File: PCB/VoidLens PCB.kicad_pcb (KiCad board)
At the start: 2 copper layers, 75 parts, among them IC1 BMI270, J1 solder pad, J2 JST-XH-2 Pin, J4 JST_XH for led Strip, J5 Programming_Pins, SW1 K3-1391A, SW2 SW_Push_DPDT, SW5 K2-1157SP-I4SW-04, U1 BQ24074RGT, U2 ATmega32U4-M, U3 NRF24L01, U5 TPS61022, U6 TPS27081ADDCR, Y1 16Mhz, Y2 16mhz

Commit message: Arrangeed components to their positions in pcb
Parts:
- R11, R12, U1: moved to B.Cu
- moved U6 127.1 mm to (225.5, 83.5)
- moved U1 117.8 mm to (201.1, 50.9), turned to 180 degrees
- moved R12 76.4 mm to (204.5, 50.9), turned to 90 degrees
- moved L7 26.2 mm to (197.5, 94.5)
- moved C1 23.4 mm to (189.0, 84.5)
- moved C2 23.4 mm to (189.0, 77.5)
- moved J2 23.4 mm to (204.5, 94.0)
- moved J4 23.4 mm to (197.0, 80.0)
- moved J5 23.4 mm to (209.5, 84.1)
- moved SW5 23.4 mm to (190.0, 94.5)
- moved R11 21.3 mm to (197.0, 50.4), turned to 90 degrees
- moved L2 19.9 mm to (107.5, 96.5)
- moved U5 15.3 mm to (208.2, 45.5)
- moved C14 5.73 mm to (167.7, 38.5)
- moved J1 1.74 mm to (196.0, 47.5)
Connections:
- C1 pad 1: batt_main -> Net-(J1-Pin_1)
- C21 pad 1: Net-(U1-IN) -> uvcc
- J1 pad 1: batt_main -> Net-(J1-Pin_1)
- SW1 pad 1: unconnected-(SW1-Pad1) -> Net-(J1-Pin_1)
- SW1 pad 2: Net-(U1-IN) -> batt_main
- SW1 pad 3: uvcc -> unconnected-(SW1-Pad3)
- U1 pad 13: Net-(U1-IN) -> uvcc
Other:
- board text added: "+"
- board text added: "-"

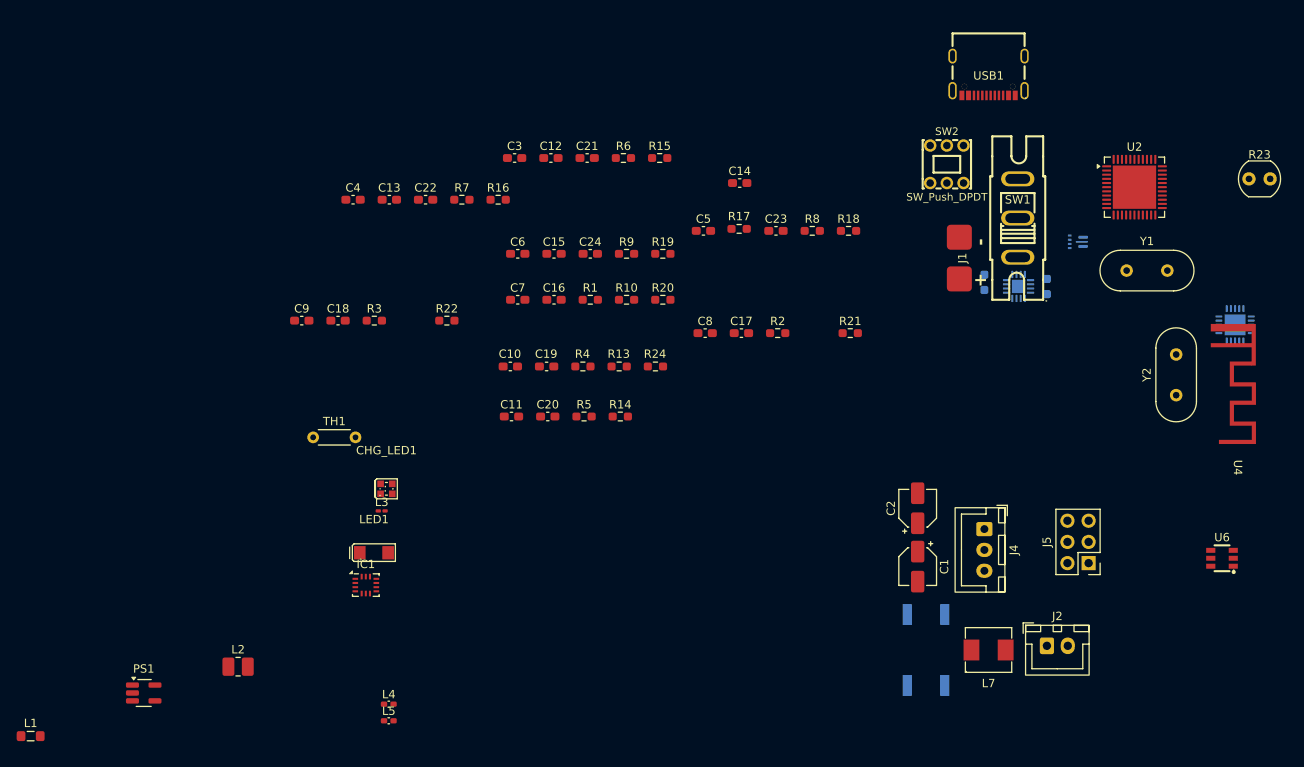
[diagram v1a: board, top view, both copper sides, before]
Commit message: routed more components in the pcb
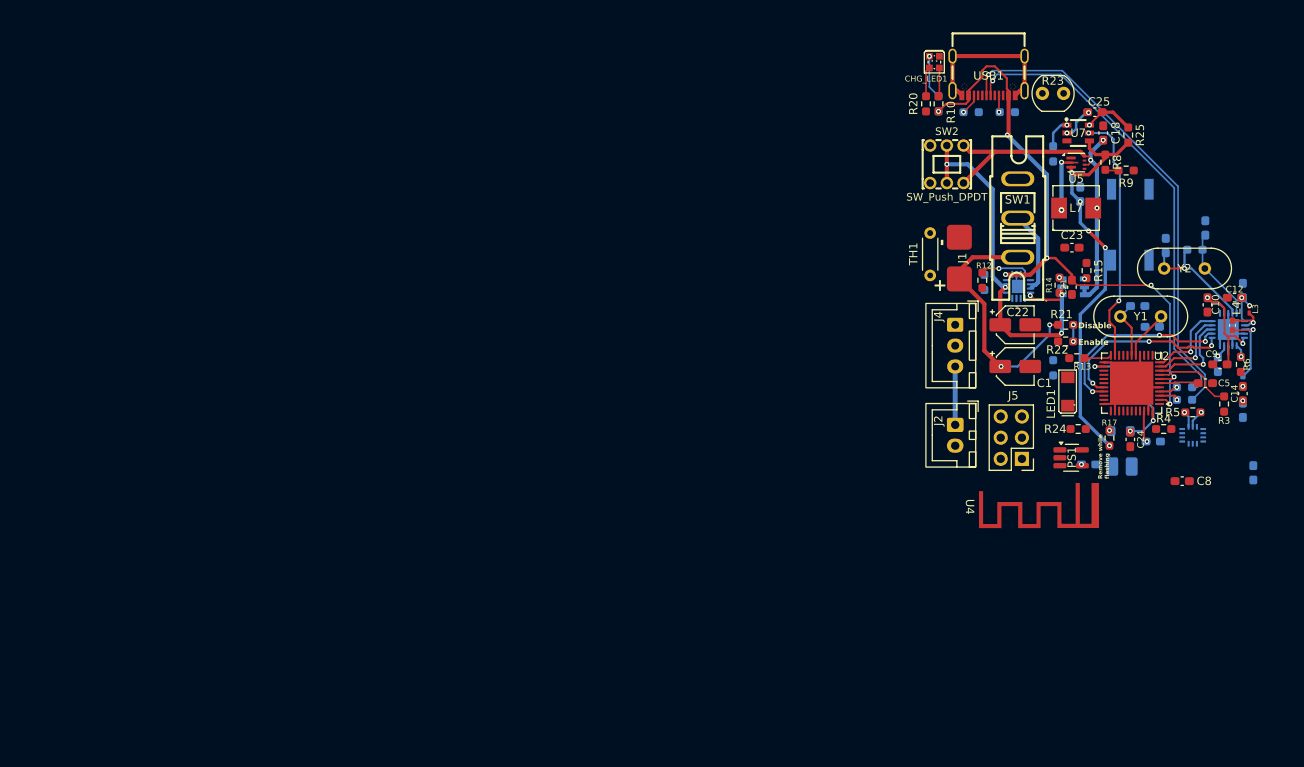
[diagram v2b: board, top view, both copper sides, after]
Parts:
- removed C2: 22uF, Capacitor_SMD:CP_Elec_4x5.4
- added C25: 0.1uF, Capacitor_SMD:C_0603_1608Metric_Pad1.08x0.95mm_HandSolder, F.Cu at (210.2, 30.0)
- added R25: 1k, Resistor_SMD:R_0603_1608Metric_Pad0.98x0.95mm_HandSolder, F.Cu at (214.2, 32.8)
- added R26: 22, Resistor_SMD:R_0603_1608Metric_Pad0.98x0.95mm_HandSolder, B.Cu at (221.0, 63.0)
- added R27: 22, Resistor_SMD:R_0603_1608Metric_Pad0.98x0.95mm_HandSolder, B.Cu at (221.0, 64.5)
- added U7: TPS27081ADDCR, lcsc_footprints:C128404_SOT-23-6_L2_9-W1_6-P0_95-LS2_8-BR, F.Cu at (208.2, 32.5)
- C11, C13, C15, C16, C17, C19, C20, C3, C4, C6, C7, IC1, L1, L2, L5, R1, R16, R19, R2, R7, U6: moved to B.Cu
- C22: footprint Capacitor_SMD:C_0603_1608Metric_Pad1.08x0.95mm_HandSolder -> Capacitor_SMD:CP_Elec_4x5.4
- R12, U5: moved to F.Cu
- R18: value 10k -> 12k; moved to B.Cu
- R3: value 110 -> 1.18k
- moved L1 135.7 mm to (213.3, 68.2)
- moved PS1 114.7 mm to (207.4, 71.5)
- moved L4 110.9 mm to (226.8, 55.6), turned to -90 degrees
- moved C9 110.2 mm to (225.2, 60.2), turned to 180 degrees
- moved L5 110.2 mm to (228.0, 62.2), turned to -90 degrees
- moved L2 108.7 mm to (213.5, 72.5)
- moved L3 106.8 mm to (228.8, 53.7), turned to 90 degrees
- moved C13 102.9 mm to (228.0, 51.4), turned to -90 degrees
- moved R3 102.4 mm to (225.8, 65.0), turned to -90 degrees
- moved IC1 100.8 mm to (222.0, 68.8), turned to 180 degrees
- moved C4 97.1 mm to (217.1, 55.8), turned to 180 degrees
- moved C18 94.5 mm to (211.2, 32.5), turned to 90 degrees
- moved C6 92.0 mm to (229.2, 73.2), turned to 90 degrees
- moved R7 88.1 mm to (222.2, 46.5), turned to 180 degrees
- moved LED1 85.4 mm to (207.0, 63.5), turned to 90 degrees
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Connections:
- C1 pad 1: Net-(J1-Pin_1) -> BQ_E
- J1 pad 1: Net-(J1-Pin_1) -> BQ_E
- R14 pad 1: GND -> Regulated_batt
- R14 pad 2: Net-(U6-R2) -> Net-(U6-R1/C1)
- R15 pad 1: Net-(U6-R1/C1) -> GND
- R15 pad 2: Regulated_batt -> Net-(U6-R2)
- R18 pad 1: 5v_en -> GND
- R18 pad 2: GND -> Net-(U7-R2)
- R21 pad 1: uvcc -> BQ_E
- SW1 pad 1: Net-(J1-Pin_1) -> BQ_E
- U2 pad 3: d- -> Net-(U2-D-)
- U2 pad 4: d+ -> Net-(U2-D+)
- U3 pad 6: IRQ -> unconnected-(U3-IRQ-Pad6)
- U5 pad 5: 5v_en -> +BATT
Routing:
- net uvcc: track 0.00 -> 75.7 mm, vias 0 -> 7
- net d-: track 0.00 -> 58.7 mm, vias 0 -> 1
- net d+: track 0.00 -> 56.1 mm, vias 0 -> 1
- net GND: track 0.00 -> 53.4 mm
- net mcu_5v: track 0.00 -> 49.6 mm, vias 0 -> 5
- net +BATT: track 0.00 -> 43.9 mm, vias 0 -> 3
- net Regulated_batt: track 0.00 -> 41.8 mm, vias 0 -> 4
- net BQ_E: track 0.00 -> 30.9 mm, vias 0 -> 2
- net 5v_en: track 0.00 -> 30.3 mm, vias 0 -> 2
- net CSN: track 0.00 -> 23.2 mm, vias 0 -> 3
- net CE: track 0.00 -> 21.7 mm, vias 0 -> 3
- net +3.3V: track 0.00 -> 16.9 mm, vias 0 -> 3
- net Net-(C24-Pad1): track 0.00 -> 16.1 mm, vias 0 -> 3
- net Net-(U3-XC2): track 0.00 -> 15.0 mm, vias 0 -> 1
- net Net-(U3-XC1): track 0.00 -> 11.2 mm
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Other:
- board text added: "Disable"
- board text added: "Enable"
- board text added: "Remove while flashing"

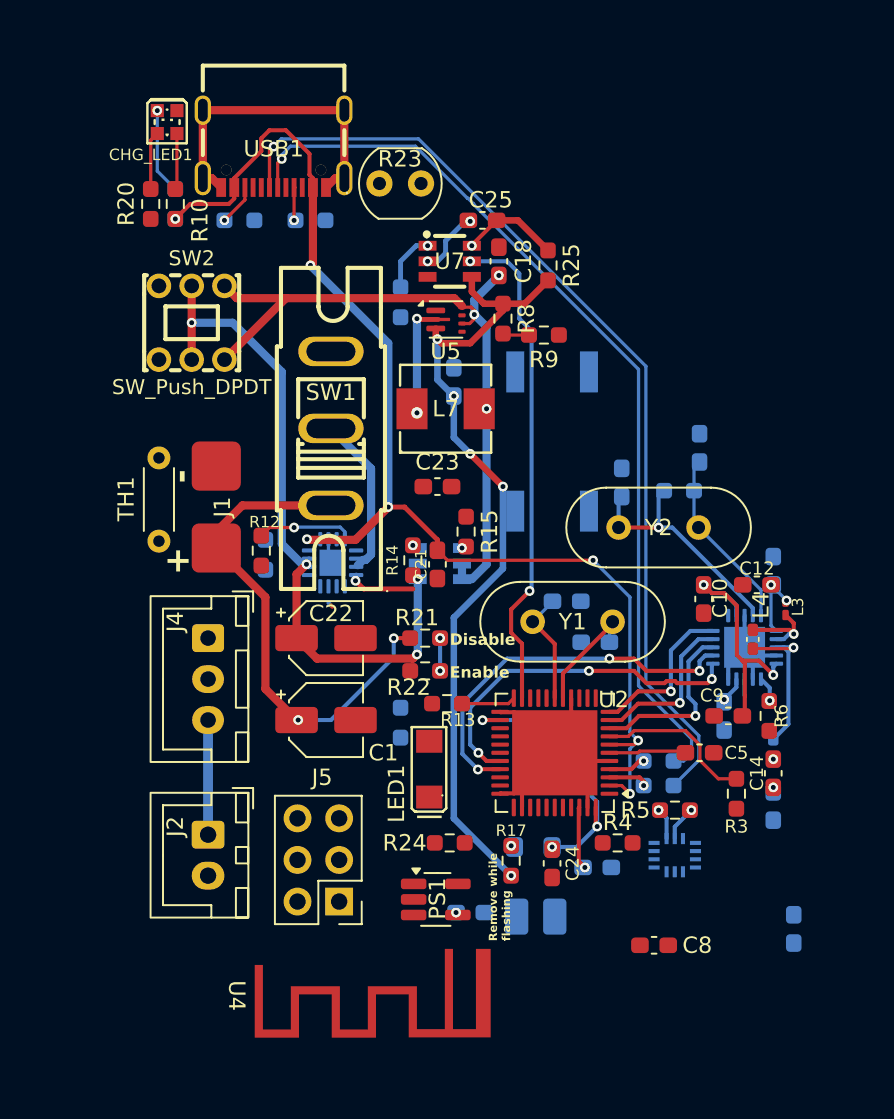
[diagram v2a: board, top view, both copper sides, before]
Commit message: finihed routing
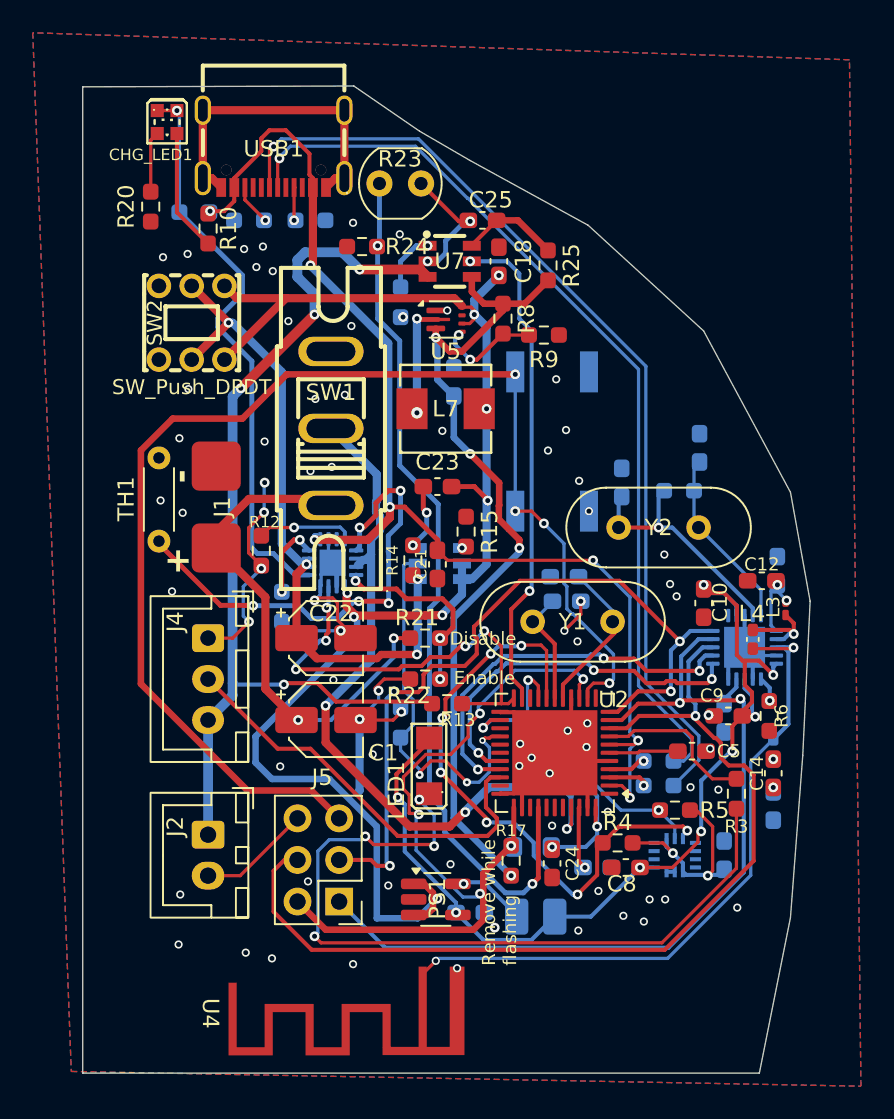
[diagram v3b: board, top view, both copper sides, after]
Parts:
- moved R24 36.8 mm to (202.9, 31.6), turned to 180 degrees
- moved C6 6.19 mm to (225.0, 68.8)
- moved C8 5.05 mm to (219.0, 69.5), turned to 0 degrees
- moved C4 4.42 mm to (215.2, 51.8)
- moved R11 3.33 mm to (198.0, 53.6)
- moved R10 2.50 mm to (193.5, 30.5), turned to -90 degrees
- moved U4 1.93 mm to (209.2, 81.0)
- moved R19 1.27 mm to (192.7, 29.5), turned to 180 degrees
- moved R2 0.59 mm to (196.0, 30.0), turned to 0 degrees
- moved R22 0.50 mm to (206.8, 58.0)
- moved C5 0.47 mm to (223.0, 62.4)
- moved C12 0.39 mm to (227.3, 52.0)
- moved C10 0.25 mm to (223.8, 53.4)
- moved C13 0.25 mm to (228.2, 51.4)
- moved LED1 0.20 mm to (207.0, 63.3)
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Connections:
- IC1 pad 1: SA0 -> unconnected-(IC1-SDO-Pad1)
- IC1 pad 4: INT1 -> unconnected-(IC1-INT1-Pad4)
- IC1 pad 9: INT2 -> unconnected-(IC1-INT2-Pad9)
- U3 pad 21: (no net) -> GND
- USB1 pad B6: d+ -> unconnected-(USB1-DP2-PadB6)
- USB1 pad B7: d- -> unconnected-(USB1-DN2-PadB7)
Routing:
- net RST: track 0.00 -> 78.8 mm, vias 0 -> 4
- net +5V: track 11.1 -> 67.6 mm, vias 2 -> 6
- net Net-(U2-PF6): track 0.00 -> 53.7 mm, vias 0 -> 2
- net SCK: track 11.1 -> 58.8 mm
- net Net-(LED1--): track 0.00 -> 47.5 mm, vias 0 -> 4
- net GND: track 53.4 -> 100.1 mm, vias 0 -> 76
- net ext_5v: track 0.00 -> 46.2 mm, vias 1 -> 5
- net +BATT: track 43.9 -> 89.5 mm, vias 3 -> 8
- net +3.3V: track 16.9 -> 59.7 mm, vias 3 -> 8
- net MOSI: track 9.97 -> 52.3 mm, vias 1 -> 2
- net MISO: track 9.82 -> 47.5 mm, vias 1 -> 4
- net IMU_SCL: track 0.00 -> 37.2 mm, vias 0 -> 7
- net batt_main: track 9.80 -> 45.0 mm, vias 0 -> 3
- net Net-(U3-ANT2): track 9.71 -> 41.0 mm, vias 1 -> 2
- net Net-(U1-~{CHG}): track 5.24 -> 34.9 mm
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- added copper zone on B.Cu, net GND
- added copper zone on F.Cu, net GND
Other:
- board outline added: 44.4 x 60.2 mm
